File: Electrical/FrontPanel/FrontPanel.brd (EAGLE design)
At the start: 88 x 46 mm, 24 parts, among them SW1 EC12E_SW

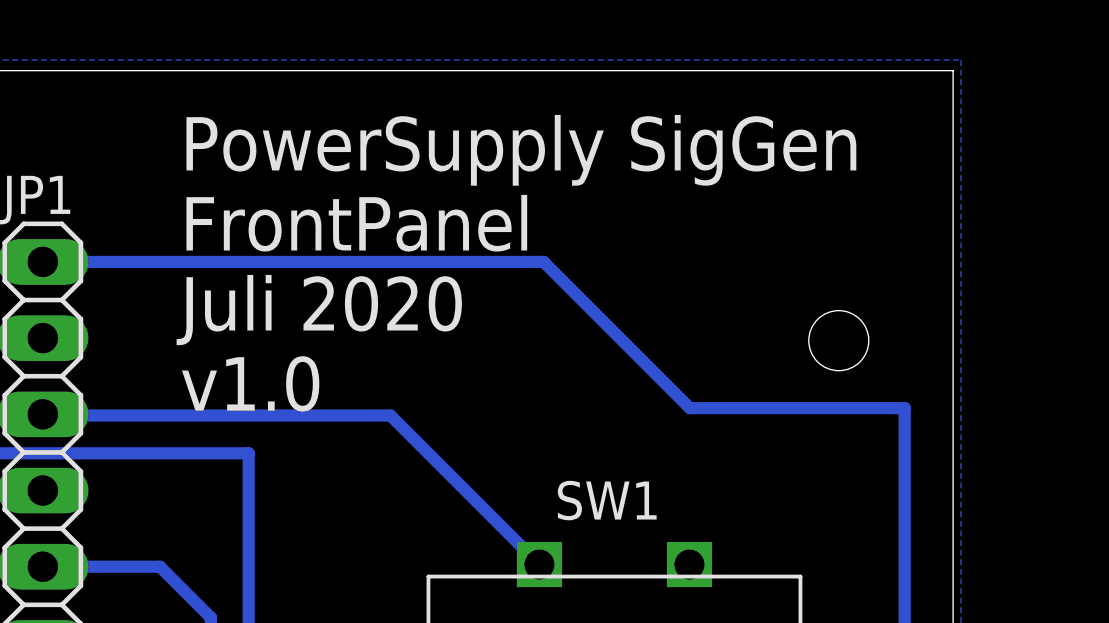
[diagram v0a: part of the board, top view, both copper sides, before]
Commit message: Updated to new project name (PS_Fgen_HW), removed Z-Diode and ATX_PWR_ON signal from MainBoard
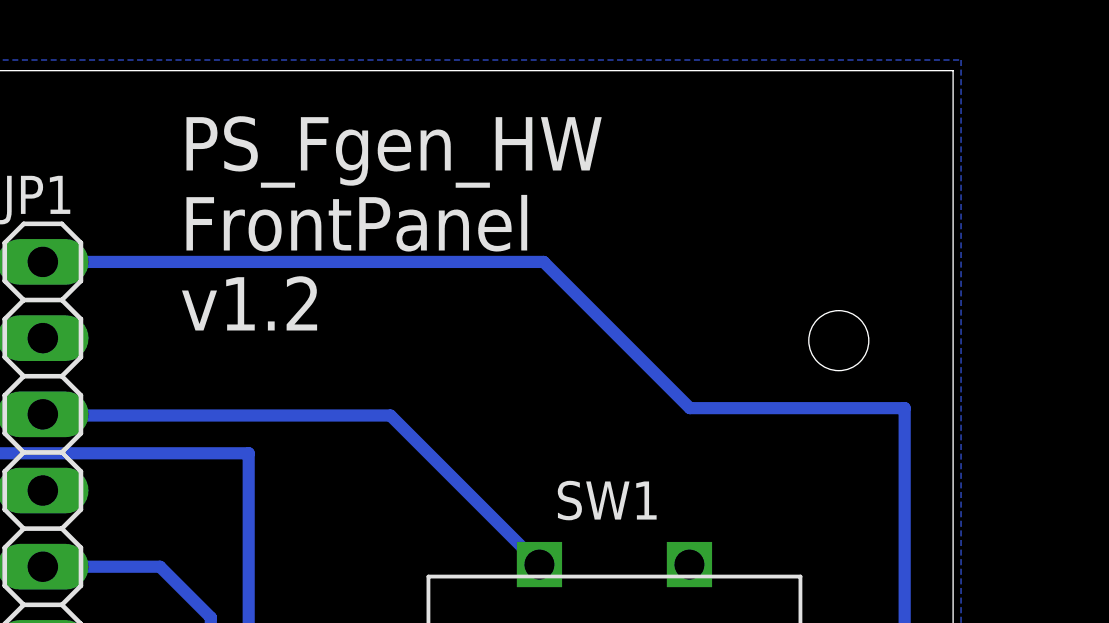
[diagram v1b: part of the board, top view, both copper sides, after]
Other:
- board text added: "PS_Fgen_HW FrontPanel v1.2"
- board text removed: "PowerSupply SigGen FrontPanel Juli 2020 v1.0"
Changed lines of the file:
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@@
 <?xml version="1.0" encoding="utf-8"?>
 <!DOCTYPE eagle SYSTEM "eagle.dtd">
-<eagle version="9.5.2">
+<eagle version="9.6.2">
 <drawing>
 <settings>
-<setting alwaysvectorfont="no"/>
+<setting alwaysvectorfont="yes"/>
 <setting verticaltext="up"/>
 </settings>
@@
 </layers>
 <board>
-<fusionsync huburn="a.YnVzaW5lc3M6bXlnbXgxMjQ4OA" projecturn="a.YnVzaW5lc3M6bXlnbXgxMjQ4OCNEMjAyMDAxMTAyNTQwMjAxNTE" f3durn="urn:adsk.wipprod:dm.lineage:h1ckcWdnRVyiVBv4xqEomw" pcbguid="a576bdb0-0f75-47d6-a048-163db8abff98" lastpulledtime="" lastsyncedchangeguid="f93fa148-d73c-a696-6ecf-d27c6a475278"/>
+<fusionsync huburn="a.YnVzaW5lc3M6bXlnbXgxMjQ4OA" projecturn="a.YnVzaW5lc3M6bXlnbXgxMjQ4OCNEMjAyMDAxMTAyNTQwMjAxNTE" f3durn="urn:adsk.wipprod:dm.lineage:h1ckcWdnRVyiVBv4xqEomw" pcbguid="a576bdb0-0f75-47d6-a048-163db8abff98" lastpulledtime="" lastsyncedchangeguid="f93fa148-d73c-a696-6ecf-d27c6a475278" latestrevisionid="" lastsyncedrevisionid="" lastboardhashguid="0a757cab-1d26-2fee-852c-39589efafcbf" lastpushedtime="2021-06-03T19:40:21Z" linktopcb3d="false"/>
 <plain>
 <wire x1="0" y1="0" x2="88" y2="0" width="0" layer="20"/>
@@
 <text x="55.88" y="8.255" size="1.778" layer="22" rot="MR0">GND</text>
 <text x="55.88" y="5.715" size="1.778" layer="22" rot="MR0">NC</text>
-<text x="62.23" y="44.45" size="1.778" layer="21" align="top-left">PowerSupply SigGen
+<text x="62.23" y="44.45" size="1.778" layer="21" align="top-left">PS_Fgen_HW
 FrontPanel
-Juli 2020
-v1.0</text>
+v1.2</text>
 </plain>
 <attributes>
